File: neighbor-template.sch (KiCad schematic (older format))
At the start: 13 parts, among them J1 NEIGHBOR1, J2 NEIGHBOR2, J7 BONUS_ROW, U1 M24C02-FMN6TP

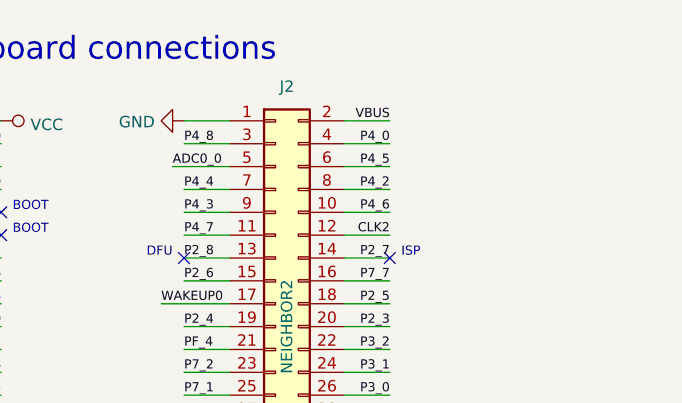
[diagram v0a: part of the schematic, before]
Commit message: change J2_P2 from VBUS to +5V fixes #8
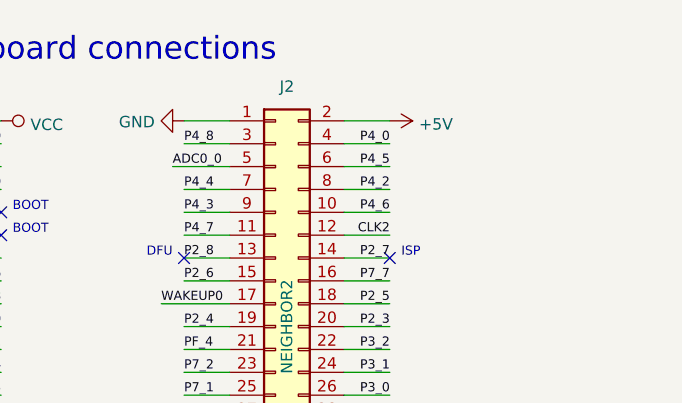
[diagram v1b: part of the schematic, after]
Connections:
- net VBUS renamed +5V
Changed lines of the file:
@@
 	1    0    0    -1
 $EndComp
-Text Label 15950 950  2    40   ~ 0
-VBUS
 $Comp
 L Connector_Generic:Conn_02x20_Odd_Even J1
@@
 Text Label 14600 3800 1    40   ~ 0
 RTCX1
+$Comp
+L power:+5V #PWR?
+U 1 1 5D89879B
+P 15950 950
+F 0 "#PWR?" H 15950 800 50  0001 C CNN
+F 1 "+5V" V 15965 1078 50  0000 L CNN
+F 2 "" H 15950 950 50  0001 C CNN
+F 3 "" H 15950 950 50  0001 C CNN
+	1    15950 950
+	0    1    1    0
+$EndComp
 $EndSCHEMATC
